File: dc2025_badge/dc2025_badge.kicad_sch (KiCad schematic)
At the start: 66 parts, among them J1 USB_C_Receptacle_USB2.0_16P, J2 Conn_ARM_JTAG_SWD_10, Q1 AO3401A, U1 TPS3808DBV, U2 STM32L053R8Tx, U5 XC6206P332MR, U6 XC6206P332MR

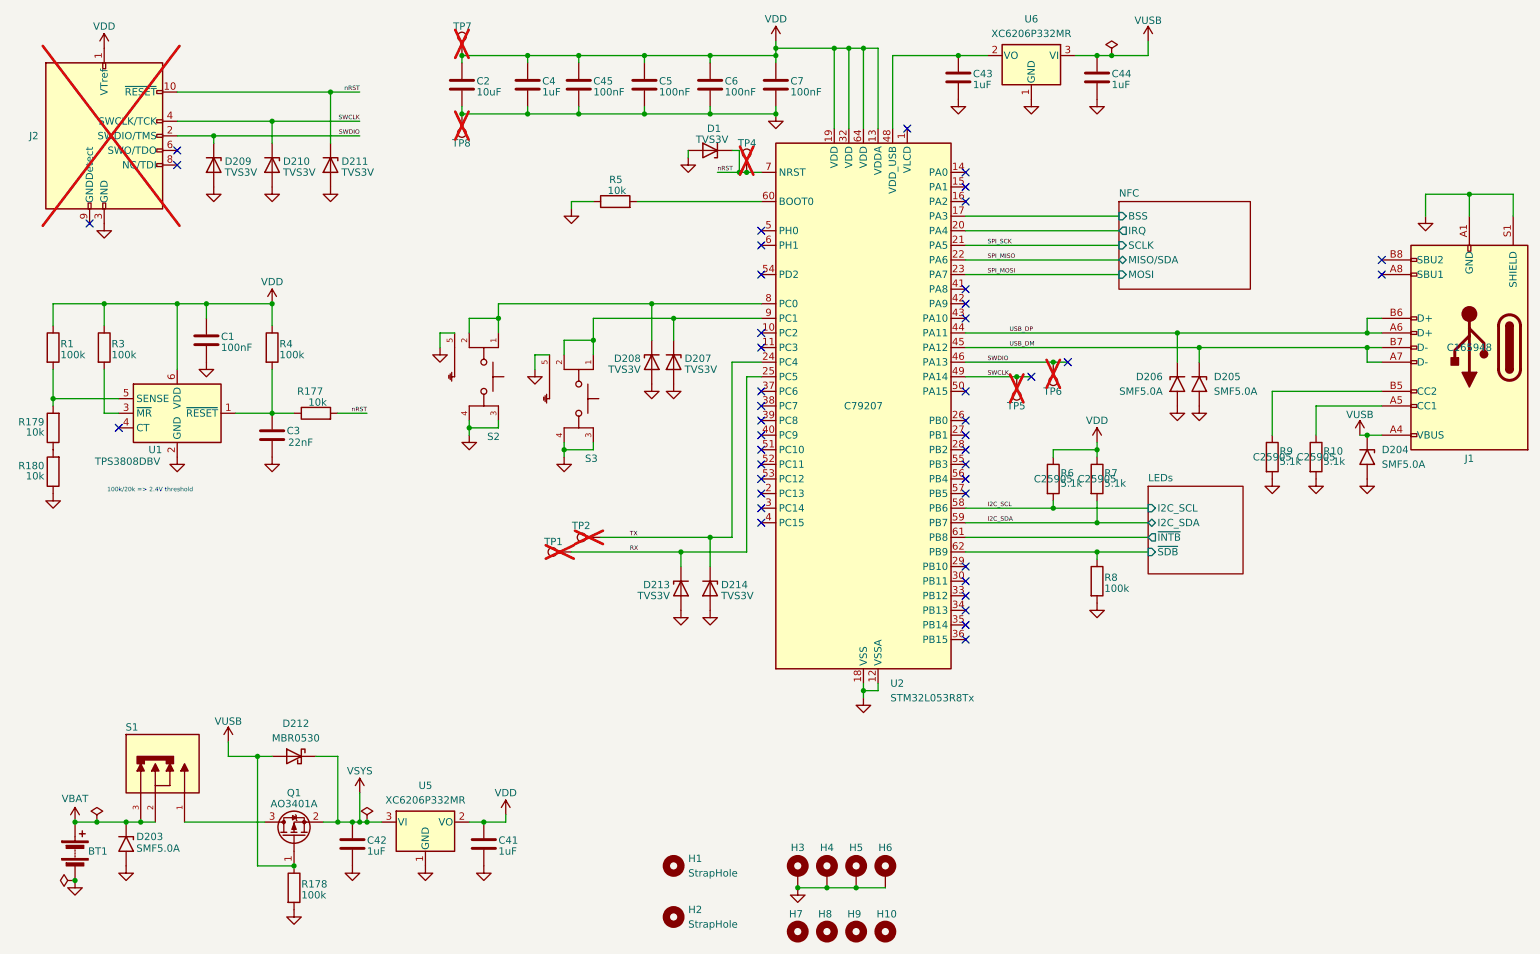
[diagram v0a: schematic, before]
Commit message: 0603 leds added, prototype version finished
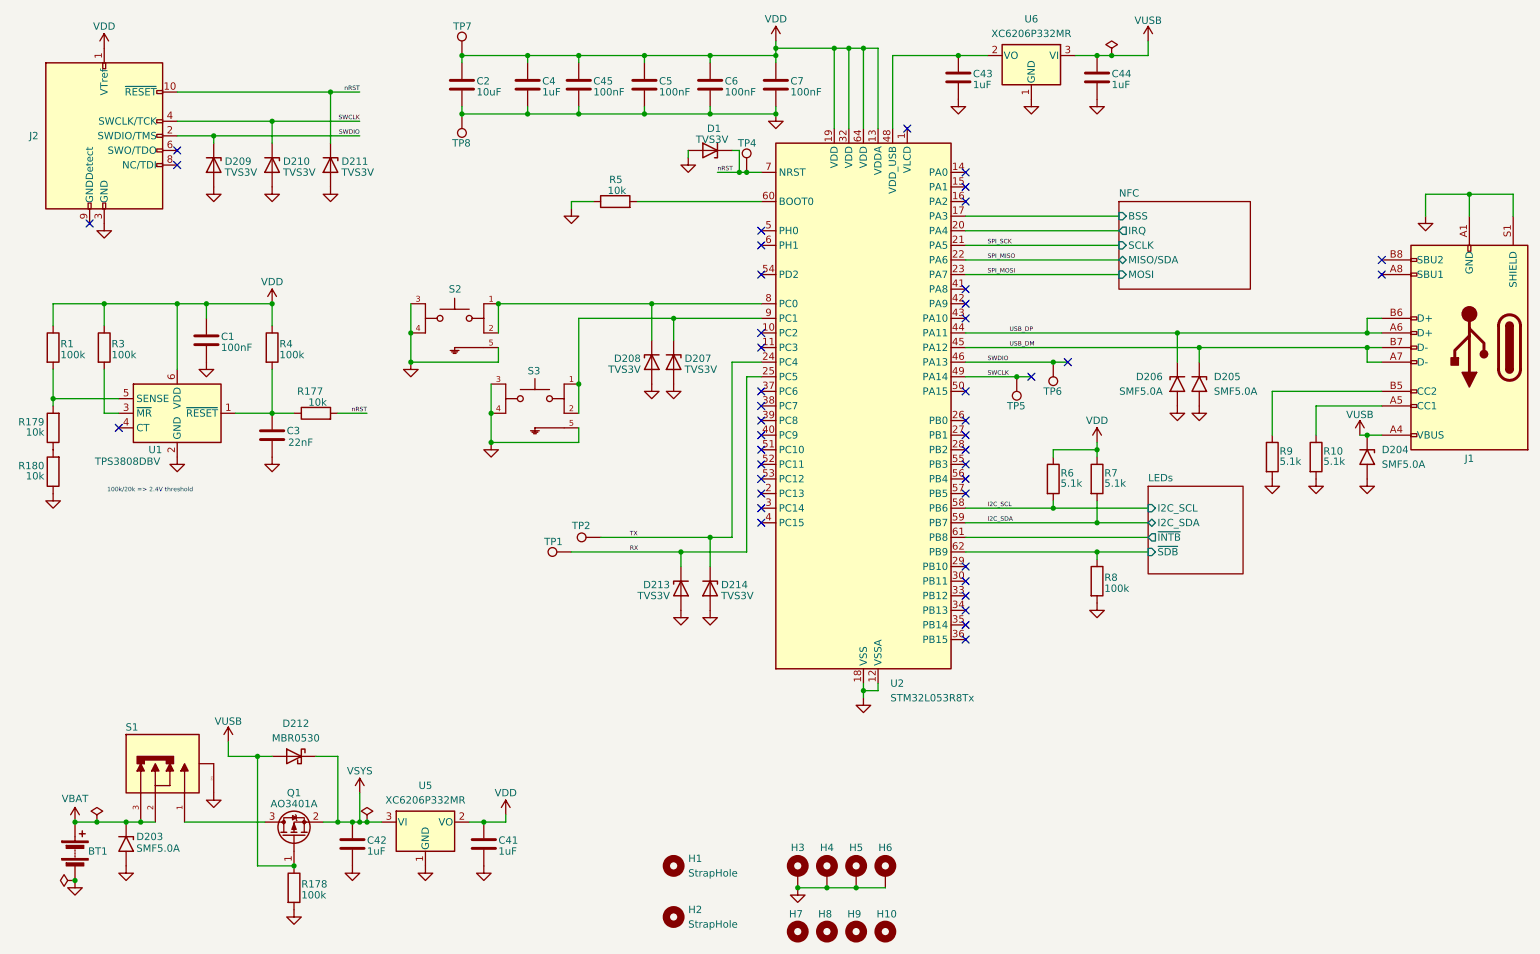
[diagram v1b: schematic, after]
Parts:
- C3: Manufacturer FH -> FH (Guangdong Fenghua Advanced Tech)
- H10, H7, H8, H9: value MountingHole -> CoverMountingHole
- H3, H4, H5, H6: value Cover mount -> Cover nut
- J1: MPN (none) -> TYPE-C-31-M-12; Manufacturer (none) -> Korean Hroparts Elec
- J2, TP1, TP2, TP4, TP5, TP6, TP7, TP8: now fitted
- R10, R6, R7, R9: MPN (none) -> 0402WGF5101TCE; Manufacturer (none) -> UNI-ROYAL(Uniroyal Elec)
- S1: Availability (none) -> In Stock; Check_prices (none) -> https://www.snapeda.com/parts/SSSS811101/ALPS/view-part/?re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; Description_1 (none) -> Switch Slide SP Side Slide 0.3A 5VDC 10000Cycles Gull Wing 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; MANUFACTURER (none) -> ALPS; MAXIMUM_PACKAGE_HEIGHT (none) -> 1.60 mm; MF (none) -> ALPS; MP (none) -> SSSS811101; PARTREV (none) -> N/A; Package (none) -> None; Price (none) -> None; STANDARD (none) -> Manufacturer Recommendations; SnapEDA_Link (none) -> https://www.snapeda.com/parts/SSSS811101/ALPS/view-part/?re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
- U2: MPN (none) -> STM32L053R8T6; Manufacturer (none) -> STMicroelectronics
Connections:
- net GND: now also S1.SH1, S1.SH2, S1.SH3, S1.SH4
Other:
- moved on the sheet: S2, S3
